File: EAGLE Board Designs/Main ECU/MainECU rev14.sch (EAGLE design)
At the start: 325 parts, among them J1 CONNECTOR-34__, J2 CONNECTOR-34__, J3 ADIS16460, K1 RELAY_DPDT_07DSMT, K2 RELAY_DPDT_07DSMT, K3 RELAY_DPDT_07DSMT, K4 RELAY_DPDT_07DSMT, K5 RELAY_DPDT_07DSMT, Q1 TRANSISTOR_N_MOS__DMG3406L-7, Q2 TRANSISTOR_P_MOS_SOT-23_DMP30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, Q3 TRANSISTOR_P_MOS_SOT-23_DMP30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, Q4 TRANSISTOR_N_MOS__DMG3406L-7, U1 MAX7400, U10 MCP3208, U11 MCP3208, U12 TCAN1051HQV-Q1, U13 TCAN1051HQV-Q1, U14 MCP3208, U15 OPAMP_1_CHANNEL_OPA991, U16 LOGICGATE_OR, U17 OPAMP_1_CHANNEL_OPA991, U18 LOGICGATE_OR, U19 OPAMP_1_CHANNEL_OPA991, U2 MAX7400, U20 LOGICGATE_OR, U21 LOGICGATE_OR, U22 OPAMP_1_CHANNEL_OPA991, U23 LOGICGATE_NOR, U24 LOGICGATE_OR, U25 OPAMP_1_CHANNEL_OPA991, U26 OPAMP_1_CHANNEL_OPA991, U27 OPAMP_1_CHANNEL_OPA991, U28 LOGICGATE_AND_DCK3, U29 OPAMP_1_CHANNEL_OPA991, U3 MAX7400, U30 OPAMP_1_CHANNEL_OPA991, U31 TCAN1051HQV-Q1, U32 TCAN1051HQV-Q1, U33 TCAN1051HQV-Q1, U34 TCAN1051HQV-Q1, U35 MAX7400, U36 MAX7400, U37 ADM8316WBX30, U38 MAX7400, U4 MAX7400, U5 VOLTAGE_REGULATOR_SOT-223_3.3V, U6 MAX7400, U7 MAX7400, U8 MAX7400, U9 MAX7400

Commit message: routing progress
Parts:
- removed C45, C49: CAPACITOR_0603_10V_0.1UF, HyTechDevices:CAPACITOR_0603_10V_0.1UF
- removed C46, C47: CAPACITOR_0603_10V_1UF, HyTechDevices:CAPACITOR_0603_10V_1UF
- removed D22: TVS__5V, HyTechDevices:TVS__5V
- removed R47: RESISTOR_0603_10K, HyTechDevices:RESISTOR_0603_10K
- removed R48: RESISTOR_0603_2.55K, HyTechDevices:RESISTOR_0603_2.55K
- removed U14: MCP3208, Temp:MCP3208
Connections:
- removed net !AD4_CS: A3.D33, U14.!CS!
- removed net 24V_SENSE_TCU: D22.C, R47.1, R48.2, U14.IN0
- removed net N$34: U14.GND
- removed net N$39: U14.VDD
- net +24V: no longer R47.2
- net +3V3: no longer C47.1, C49.1, U14.VREF
- net +5V: no longer C45.1, C46.1
- net 24V_SENSE_ECU: now also A3.A12
- net CURRENT: now also A3.A15; no longer U14.IN1
- net GND: no longer C45.2, C46.2, C47.2, C49.2, D22.A, R48.1, U14.AGND
- net REFERENCE: now also A3.A14; no longer U14.IN2
- net TELEM_CLK: no longer U14.CLK
- net TELEM_SDI: no longer U14.SDO
- net TELEM_SDO: no longer U14.SDI

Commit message: routing progress
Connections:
- new net STEERING_1_PRE: R41.2, R42.2, U8.IN
- net SHDN_B_READ: now also A2.A10; no longer A2.D3
- net SHDN_C_READ: now also A2.A17; no longer A2.D4
- net SHDN_D_READ: now also A2.A16; no longer A2.D5
- net SHDN_E_READ: now also A2.A15; no longer A2.D6
- net STEERING_1_EXT: no longer R41.2, R42.2, U8.IN
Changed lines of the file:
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@@
 <net name="SHDN_B_READ" class="0">
 <segment>
-<wire x1="233.68" y1="83.82" x2="241.3" y2="83.82" width="0.1524" layer="91"/>
-<label x="241.3" y="83.82" size="1.27" layer="95" xref="yes"/>
-<pinref part="A2" gate="G$1" pin="D3"/>
+<wire x1="200.66" y1="121.92" x2="208.28" y2="121.92" width="0.1524" layer="91"/>
+<label x="200.66" y="121.92" size="1.27" layer="95" rot="R180" xref="yes"/>
+<pinref part="A2" gate="G$1" pin="A10"/>
 </segment>
 </net>
 <net name="SHDN_C_READ" class="0">
 <segment>
-<wire x1="233.68" y1="86.36" x2="241.3" y2="86.36" width="0.1524" layer="91"/>
-<label x="241.3" y="86.36" size="1.27" layer="95" xref="yes"/>
-<pinref part="A2" gate="G$1" pin="D4"/>
+<wire x1="200.66" y1="109.22" x2="208.28" y2="109.22" width="0.1524" layer="91"/>
+<pinref part="A2" gate="G$1" pin="A17"/>
+<label x="200.66" y="109.22" size="1.27" layer="95" rot="R180" xref="yes"/>
 </segment>
 </net>
 <net name="SHDN_D_READ" class="0">
 <segment>
-<wire x1="233.68" y1="88.9" x2="241.3" y2="88.9" width="0.1524" layer="91"/>
-<label x="241.3" y="88.9" size="1.27" layer="95" xref="yes"/>
-<pinref part="A2" gate="G$1" pin="D5"/>
+<wire x1="200.66" y1="111.76" x2="208.28" y2="111.76" width="0.1524" layer="91"/>
+<pinref part="A2" gate="G$1" pin="A16"/>
+<label x="200.66" y="111.76" size="1.27" layer="95" rot="R180" xref="yes"/>
 </segment>
 </net>
 <net name="SHDN_E_READ" class="0">
 <segment>
-<wire x1="233.68" y1="91.44" x2="241.3" y2="91.44" width="0.1524" layer="91"/>
-<label x="241.3" y="91.44" size="1.27" layer="95" xref="yes"/>
-<pinref part="A2" gate="G$1" pin="D6"/>
+<wire x1="200.66" y1="114.3" x2="208.28" y2="114.3" width="0.1524" layer="91"/>
+<pinref part="A2" gate="G$1" pin="A15"/>
+<label x="200.66" y="114.3" size="1.27" layer="95" rot="R180" xref="yes"/>
 </segment>
 </net>
@@
 <net name="STEERING_1_EXT" class="0">
 <segment>
-<pinref part="R42" gate="G$1" pin="2"/>
-<wire x1="172.72" y1="83.82" x2="172.72" y2="81.28" width="0.1524" layer="91"/>
-<pinref part="U8" gate="G$1" pin="IN"/>
-<wire x1="172.72" y1="83.82" x2="198.12" y2="83.82" width="0.1524" layer="91"/>
-<junction x="172.72" y="83.82"/>
-<wire x1="170.18" y1="83.82" x2="172.72" y2="83.82" width="0.1524" layer="91"/>
-<pinref part="R41" gate="G$1" pin="2"/>
-</segment>
-<segment>
 <wire x1="160.02" y1="83.82" x2="162.56" y2="83.82" width="0.1524" layer="91"/>
 <label x="160.02" y="83.82" size="1.27" layer="95" rot="R180" xref="yes"/>
@@
 </segment>
 </net>
+<net name="STEERING_1_PRE" class="0">
+<segment>
+<pinref part="R41" gate="G$1" pin="2"/>
+<pinref part="U8" gate="G$1" pin="IN"/>
+<wire x1="170.18" y1="83.82" x2="172.72" y2="83.82" width="0.1524" layer="91"/>
+<pinref part="R42" gate="G$1" pin="2"/>
+<wire x1="172.72" y1="83.82" x2="198.12" y2="83.82" width="0.1524" layer="91"/>
+<wire x1="172.72" y1="81.28" x2="172.72" y2="83.82" width="0.1524" layer="91"/>
+<junction x="172.72" y="83.82"/>
+</segment>
+</net>

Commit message: passed DRC
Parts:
- added TP10, TP9: TEST_POINT, HyTechDevices:TEST_POINT
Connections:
- net CURRENT: now also TP9.1
- net REFERENCE: now also TP10.1
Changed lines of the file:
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@@
 <part name="R23" library="HyTechDevices" deviceset="RESISTOR_?_*" device="0603" technology="10K"/>
 <part name="R41" library="HyTechDevices" deviceset="RESISTOR_?_*" device="0603" technology="10K"/>
+<part name="TP9" library="HyTechDevices" deviceset="TEST_POINT" device=""/>
+<part name="TP10" library="HyTechDevices" deviceset="TEST_POINT" device=""/>
 </parts>
 <sheets>
@@
 <attribute name="RESISTANCE" x="166.37" y="82.55" size="1.27" layer="96" align="top-center"/>
 </instance>
+<instance part="TP9" gate="G$1" x="96.52" y="185.42" smashed="yes" rot="R180">
+<attribute name="NAME" x="99.06" y="183.642" size="1.27" layer="95" rot="R180"/>
+<attribute name="MPN" x="99.06" y="187.198" size="1.27" layer="95" rot="R180" align="top-left"/>
+</instance>
+<instance part="TP10" gate="G$1" x="96.52" y="157.48" smashed="yes" rot="R180">
+<attribute name="NAME" x="99.06" y="155.702" size="1.27" layer="95" rot="R180"/>
+<attribute name="MPN" x="99.06" y="159.258" size="1.27" layer="95" rot="R180" align="top-left"/>
+</instance>
 </instances>
 <busses>
@@
 <segment>
 <pinref part="U3" gate="G$1" pin="OUT"/>
-<wire x1="88.9" y1="185.42" x2="91.44" y2="185.42" width="0.1524" layer="91"/>
 <label x="91.44" y="185.42" size="1.27" layer="95" xref="yes"/>
+<pinref part="TP9" gate="G$1" pin="1"/>
+<wire x1="93.98" y1="185.42" x2="88.9" y2="185.42" width="0.1524" layer="91"/>
 </segment>
 </net>
@@
 <segment>
 <pinref part="U9" gate="G$1" pin="OUT"/>
-<wire x1="88.9" y1="157.48" x2="91.44" y2="157.48" width="0.1524" layer="91"/>
 <label x="91.44" y="157.48" size="1.27" layer="95" xref="yes"/>
+<pinref part="TP10" gate="G$1" pin="1"/>
+<wire x1="93.98" y1="157.48" x2="88.9" y2="157.48" width="0.1524" layer="91"/>
 </segment>
 </net>

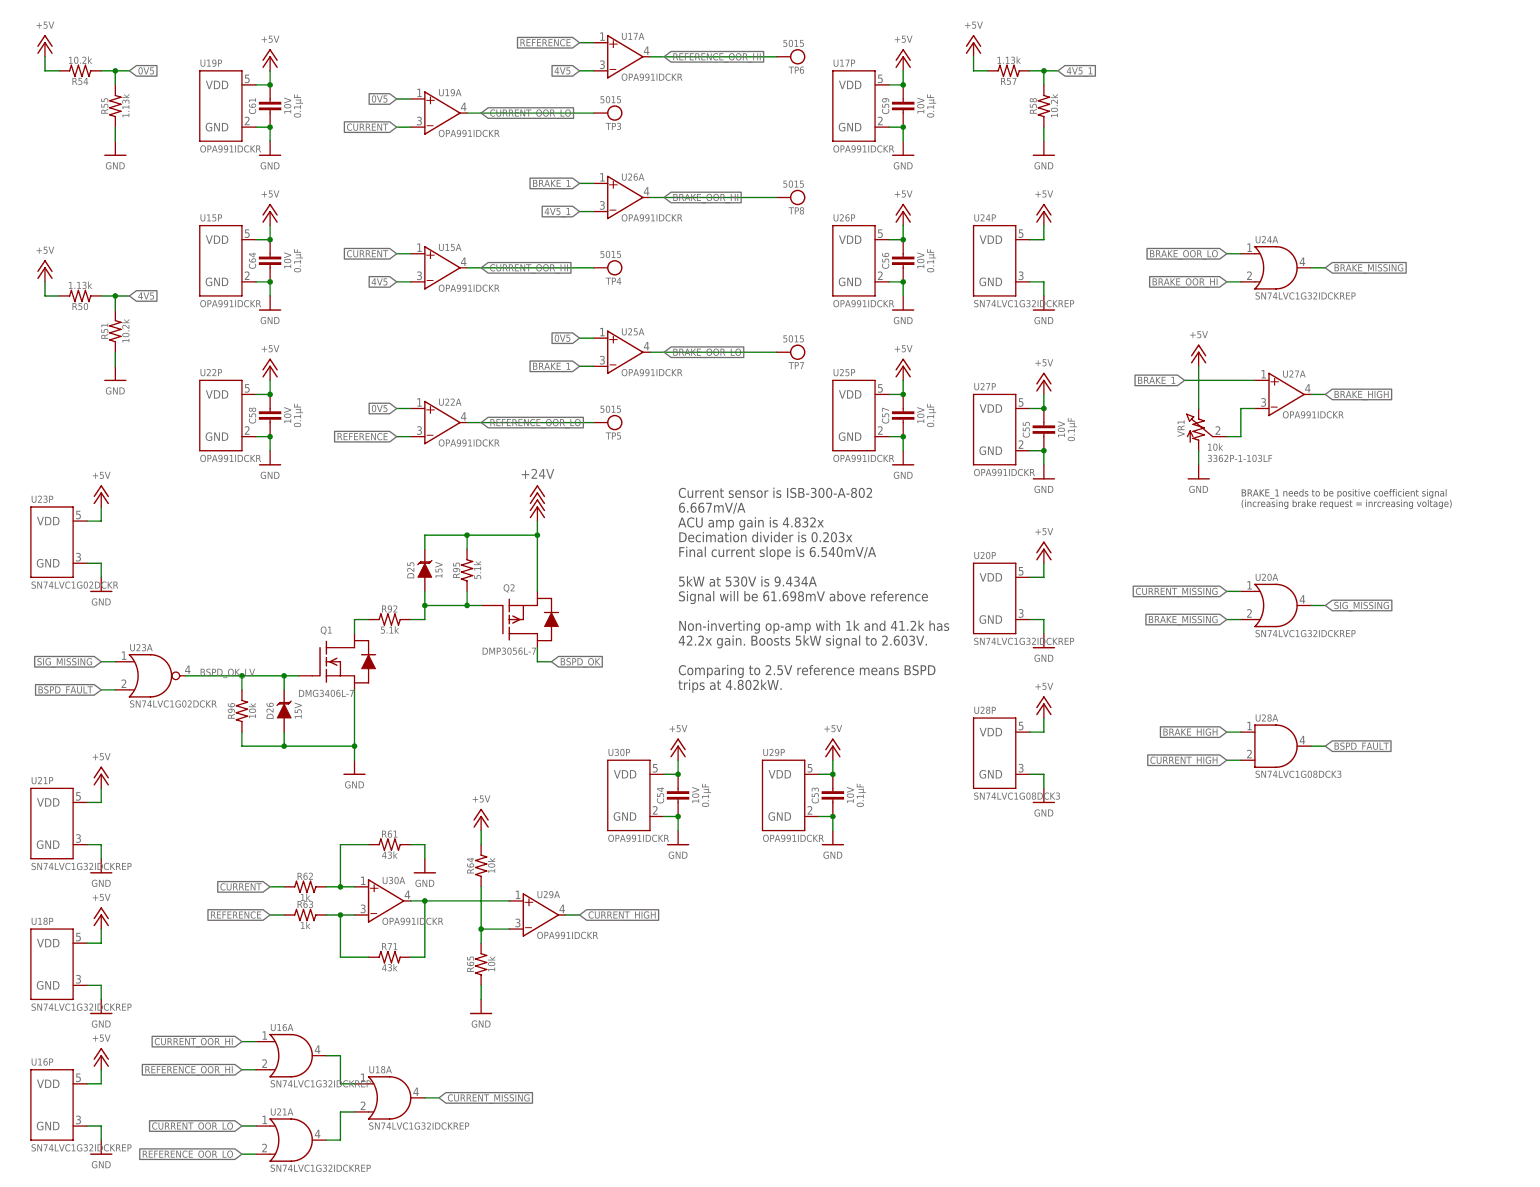
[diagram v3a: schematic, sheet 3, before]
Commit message: updated resistors. updated BSPD. passed DRC
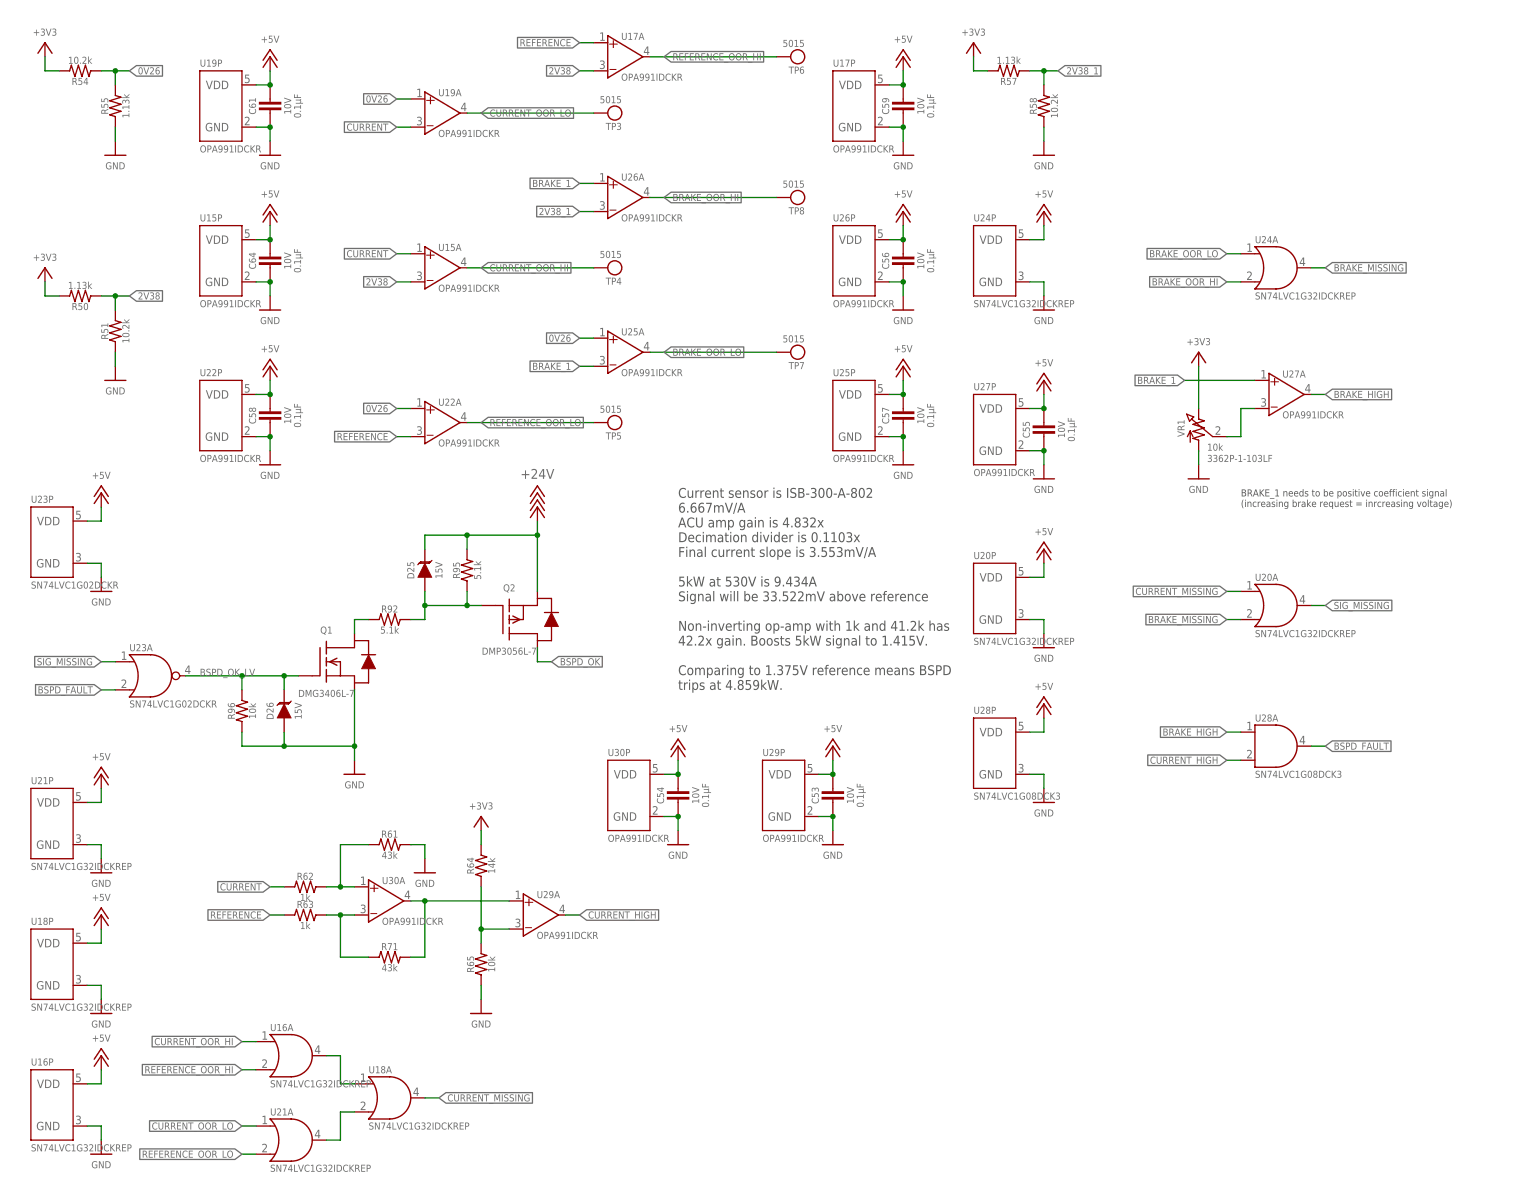
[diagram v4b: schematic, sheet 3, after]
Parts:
- R101, R75, R79, R83: value RESISTOR_0603_13K -> RESISTOR_0603_10K; device HyTechDevices:RESISTOR_0603_13K -> HyTechDevices:RESISTOR_0603_10K
- R64: value RESISTOR_0603_10K -> RESISTOR_0603_14K; device HyTechDevices:RESISTOR_0603_10K -> HyTechDevices:RESISTOR_0603_14K
- R74, R78, R82, R99: value RESISTOR_0603_3.3K -> RESISTOR_0603_1.24K; device HyTechDevices:RESISTOR_0603_3.3K -> HyTechDevices:RESISTOR_0603_1.24K
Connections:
- net 0V5 renamed 0V26
- net 4V5 renamed 2V38
- net 4V5_1 renamed 2V38_1
- net +3V3: now also R50.2, R54.2, R57.2, R64.2, VR1.2
- net +5V: no longer R50.2, R54.2, R57.2, R64.2, VR1.2
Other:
- note added: "Current sensor is ISB-300-A-802 6.667mV/A ACU amp gain is 4.832x Decimation divider is 0.1103x Final current slope is 3.553mV/A 5kW at 530V is 9.434A Signal will be 33.522mV above reference Non-inverting op-amp with 1k and 41.2k has 42.2x gain. Boosts 5kW signal to 1.415V. Comparing to 1.375V reference means BSPD trips at 4.859kW."
- note removed: "Current sensor is ISB-300-A-802 6.667mV/A ACU amp gain is 4.832x Decimation divider is 0.203x Final current slope is 6.540mV/A 5kW at 530V is 9.434A Signal will be 61.698mV above reference Non-inverting op-amp with 1k and 41.2k has 42.2x gain. Boosts 5kW signal to 2.603V. Comparing to 2.5V reference means BSPD trips at 4.802kW."

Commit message: design review changes
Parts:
- D5: DKPN (none) -> GSOT03-E3-08CT-ND; MOPN (none) -> 78-GSOT03-E3-08; MPN (none) -> GSOT03-E3-08; VOLTAGE (none) -> 3.3V
- R1: value RESISTOR_0603_2.55K -> RESISTOR_0603_1.24K; device HyTechDevices:RESISTOR_0603_2.55K -> HyTechDevices:RESISTOR_0603_1.24K
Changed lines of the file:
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@@
 <part name="P264" library="HyTechSupplies" deviceset="+24V" device=""/>
 <part name="R2" library="HyTechDevices" deviceset="RESISTOR_?_*" device="0603" technology="10K"/>
-<part name="R1" library="HyTechDevices" deviceset="RESISTOR_?_*" device="0603" technology="2.55K"/>
+<part name="R1" library="HyTechDevices" deviceset="RESISTOR_?_*" device="0603" technology="1.24K" value="RESISTOR_0603_1.24K"/>
 <part name="P265" library="HyTechSupplies" deviceset="GND" device=""/>
-<part name="D5" library="HyTechDevices" deviceset="TVS_?_*" device="" technology="5V"/>
+<part name="D5" library="HyTechDevices" deviceset="TVS_?_*" device="" technology="5V">
+<attribute name="DKPN" value="GSOT03-E3-08CT-ND"/>
+<attribute name="MOPN" value="78-GSOT03-E3-08"/>
+<attribute name="MPN" value="GSOT03-E3-08"/>
+<attribute name="VOLTAGE" value="3.3V"/>
+</part>
 <part name="P302" library="HyTechSupplies" deviceset="GND" device=""/>
 <part name="P303" library="HyTechSupplies" deviceset="GND" device=""/>
